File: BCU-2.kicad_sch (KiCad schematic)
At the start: 9 parts, among them J2 Conn_01x12_Male, J6 Conn_01x04_Male, U1 Teensy3.2

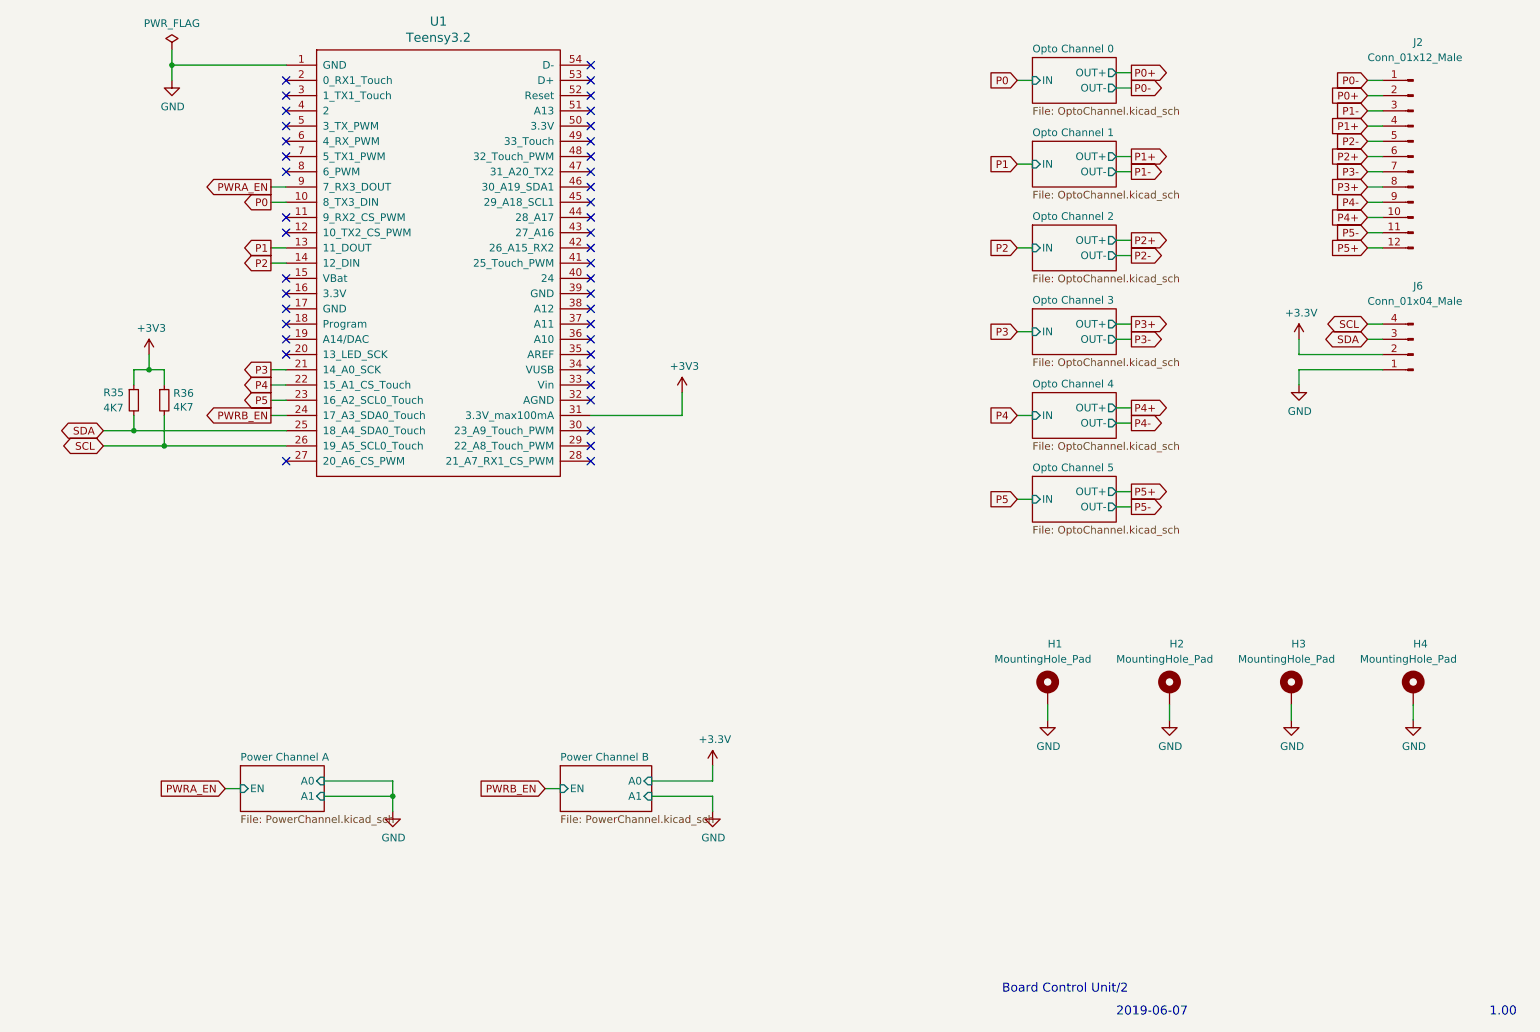
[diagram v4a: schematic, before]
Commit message: Schematic: Replace Teensy 3.2 by PCF8574
Signed-off-by: Geert Uytterhoeven <geert@linux-m68k.org>
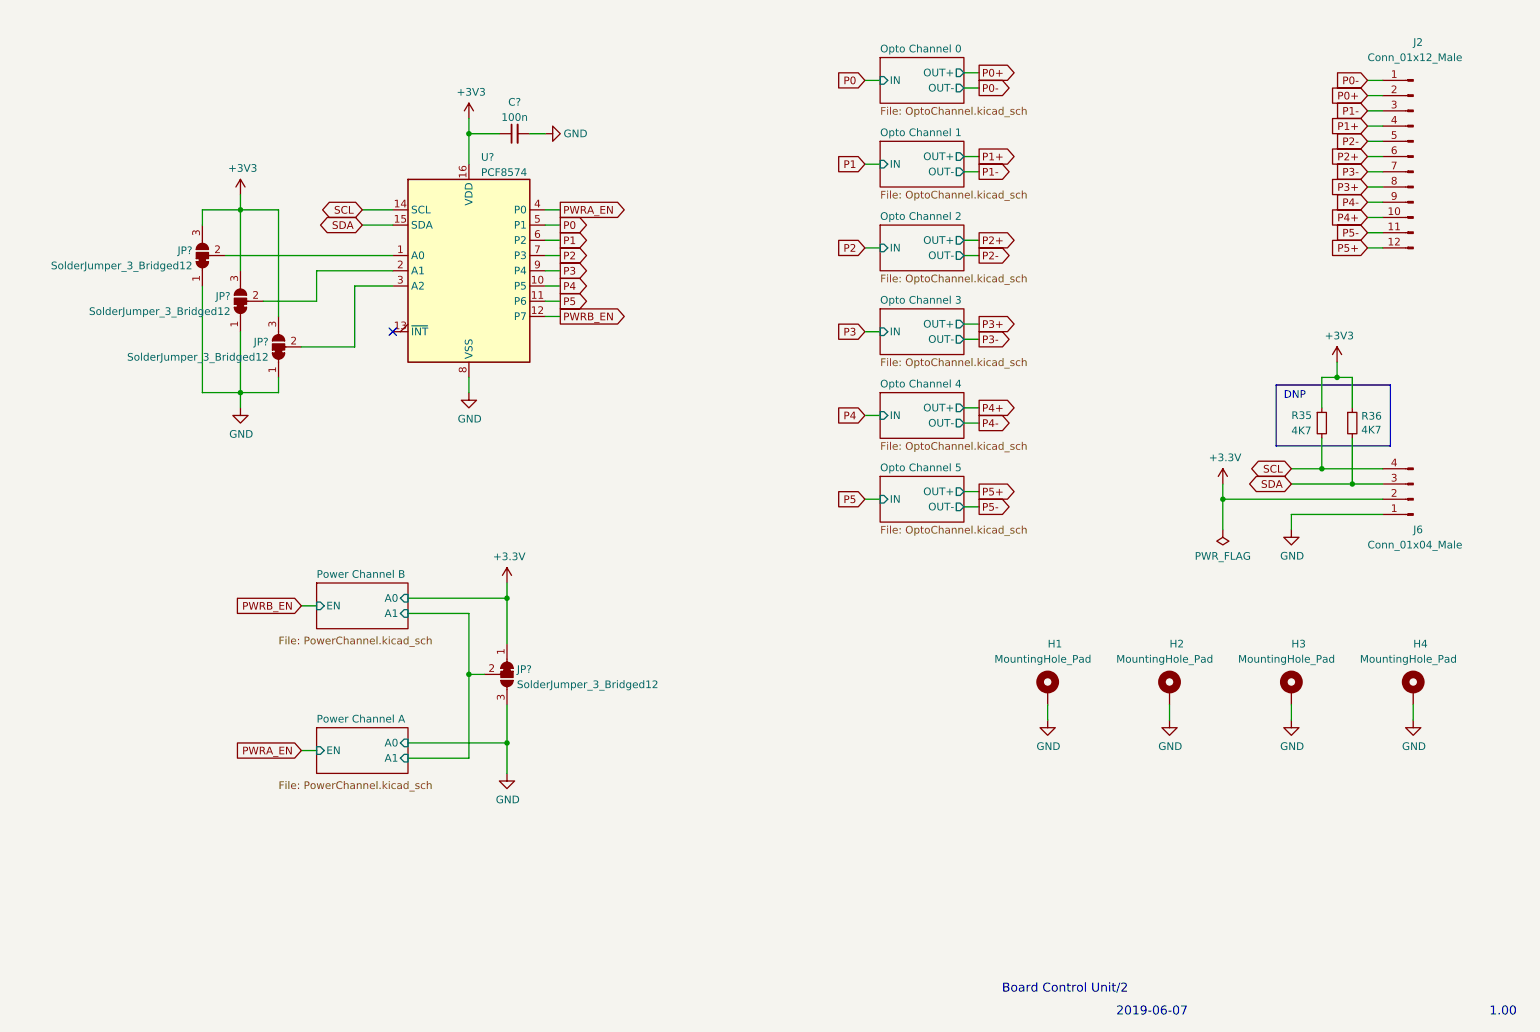
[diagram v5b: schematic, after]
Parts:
- removed U1: Teensy3.2, teensy:Teensy32-DIP28, symbol teensy:Teensy3.2
- added C?: 100n, Capacitor_SMD:C_0603_1608Metric_Pad1.05x0.95mm_HandSolder, symbol Device:C_Small
- added JP? (x4): SolderJumper_3_Bridged12, symbol Jumper:SolderJumper_3_Bridged12
- added U?: PCF8574, symbol Interface_Expansion:PCF8574
- R35, R36: now left out of the parts list
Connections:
- net +3V3: now also C?.1, JP?.1 (A), JP?.3 (B), JP?.3 (B), JP?.3 (B), U?.16 (VDD)
- net GND: now also C?.2, JP?.1 (A), JP?.1 (A), JP?.1 (A), JP?.3 (B), U?.8 (VSS)
- net P0: now also U?.5 (P1)
- net P1: now also U?.6 (P2)
- net P2: now also U?.7 (P3)
- net P3: now also U?.9 (P4)
- net P4: now also U?.10 (P5)
- net P5: now also U?.11 (P6)
- net PWRA_EN: now also U?.4 (P0)
- net PWRB_EN: now also U?.12 (P7)
- net SCL: now also R35.2, U?.14 (SCL); no longer R36.2
- net SDA: now also R36.2, U?.15 (SDA); no longer R35.2
- new net: JP?.2 (C), U?.1 (A0)
- new net: JP?.2 (C), U?.3 (A2)
- new net: JP?.2 (C), U?.2 (A1)
- new net Power Channel A/A1: JP?.2 (C)
- no-connect marks 42 -> 1
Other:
- note added: "DNP"
- moved on the sheet: J6, R35, R36

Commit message: Schematic: Renumber Power and Opto Channels
Renumber Power Channels to C-D, and Opto Channels to 6-11, to
avoid ambiguity with the channel numbers on the base BCU/2.

Signed-off-by: Geert Uytterhoeven <geert@linux-m68k.org>
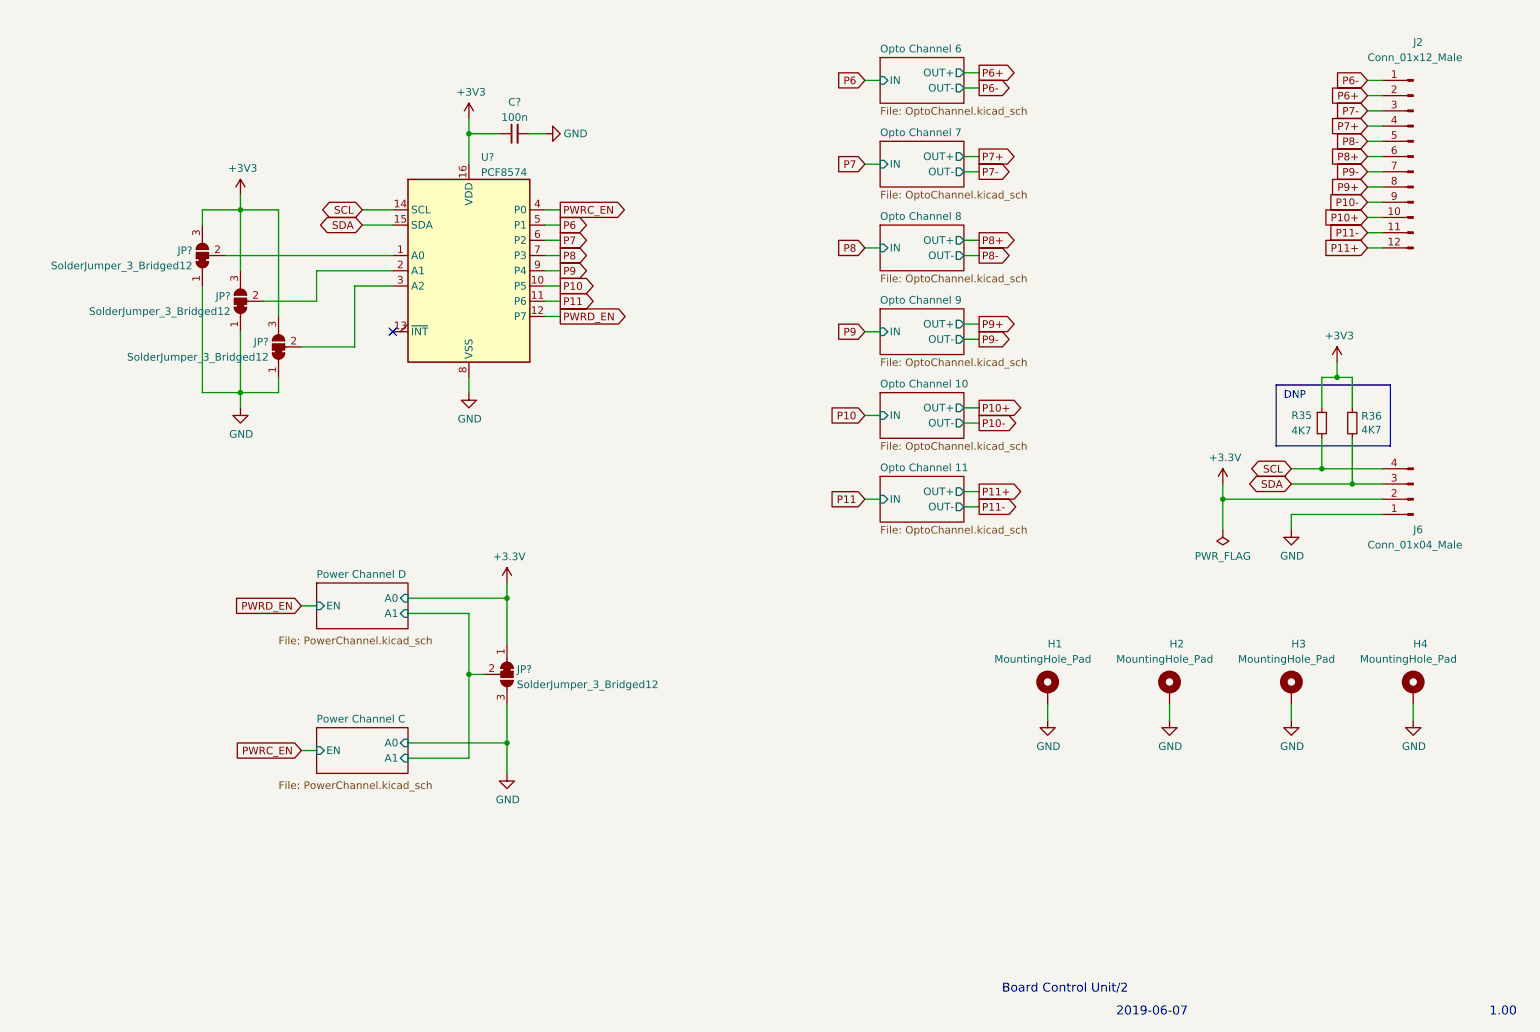
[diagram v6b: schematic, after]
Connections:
- net P0 renamed P6
- net P0+ renamed P6+
- net P0- renamed P6-
- net P1 renamed P7
- net P1+ renamed P7+
- net P1- renamed P7-
- net P2 renamed P8
- net P2+ renamed P8+
- net P2- renamed P8-
- net P3 renamed P9
- net P3+ renamed P9+
- net P3- renamed P9-
- net P4 renamed P10
- net P4+ renamed P10+
- net P4- renamed P10-
- net P5 renamed P11
- net P5+ renamed P11+
- net P5- renamed P11-
- net PWRA_EN renamed PWRC_EN
- net PWRB_EN renamed PWRD_EN
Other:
- sheet Opto Channel 0 renamed Opto Channel 6
- sheet Opto Channel 1 renamed Opto Channel 7
- sheet Opto Channel 2 renamed Opto Channel 8
- sheet Opto Channel 3 renamed Opto Channel 9
- sheet Opto Channel 4 renamed Opto Channel 10
- sheet Opto Channel 5 renamed Opto Channel 11
- sheet Power Channel A renamed Power Channel C
- sheet Power Channel B renamed Power Channel D

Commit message: Schematic: Annotate symbol references
Fill in schematic symbol reference designators.

Signed-off-by: Geert Uytterhoeven <geert@linux-m68k.org>
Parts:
- gave numbers to parts that had none: 6
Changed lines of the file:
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@@
   (symbol (lib_id "Jumper:SolderJumper_3_Bridged12") (at 105.41 137.16 270) (unit 1)
     (in_bom yes) (on_board yes) (fields_autoplaced)
-    (property "Reference" "JP?" (id 0) (at 107.061 136.3253 90)
+    (property "Reference" "JP4" (id 0) (at 107.061 136.3253 90)
       (effects (font (size 1.27 1.27)) (justify left))
     )
@@
   (symbol (lib_id "Jumper:SolderJumper_3_Bridged12") (at 54.61 67.31 90) (unit 1)
     (in_bom yes) (on_board yes) (fields_autoplaced)
-    (property "Reference" "JP?" (id 0) (at 52.9591 66.4753 90)
+    (property "Reference" "JP1" (id 0) (at 52.9591 66.4753 90)
       (effects (font (size 1.27 1.27)) (justify left))
     )
@@
   (symbol (lib_id "power:GND") (at 60.96 92.71 0) (unit 1)
     (in_bom yes) (on_board yes)
-    (property "Reference" "#PWR?" (id 0) (at 60.96 99.06 0)
+    (property "Reference" "#PWR02" (id 0) (at 60.96 99.06 0)
       (effects (font (size 1.27 1.27)) hide)
     )
@@
   (symbol (lib_id "power:GND") (at 111.76 46.99 90) (unit 1)
     (in_bom yes) (on_board yes)
-    (property "Reference" "#PWR?" (id 0) (at 118.11 46.99 0)
+    (property "Reference" "#PWR010" (id 0) (at 118.11 46.99 0)
       (effects (font (size 1.27 1.27)) hide)
     )
@@
   (symbol (lib_id "power:+3V3") (at 60.96 57.15 0) (unit 1)
     (in_bom yes) (on_board yes)
-    (property "Reference" "#PWR?" (id 0) (at 60.96 60.96 0)
+    (property "Reference" "#PWR01" (id 0) (at 60.96 60.96 0)
       (effects (font (size 1.27 1.27)) hide)
     )
@@
   (symbol (lib_id "Jumper:SolderJumper_3_Bridged12") (at 67.31 82.55 90) (unit 1)
     (in_bom yes) (on_board yes) (fields_autoplaced)
-    (property "Reference" "JP?" (id 0) (at 65.6591 81.7153 90)
+    (property "Reference" "JP3" (id 0) (at 65.6591 81.7153 90)
       (effects (font (size 1.27 1.27)) (justify left))
     )
@@
   (symbol (lib_id "Interface_Expansion:PCF8574") (at 99.06 69.85 0) (unit 1)
     (in_bom yes) (on_board yes) (fields_autoplaced)
-    (property "Reference" "U?" (id 0) (at 101.0794 50.9102 0)
+    (property "Reference" "U1" (id 0) (at 101.0794 50.9102 0)
       (effects (font (size 1.27 1.27)) (justify left))
     )
@@
   (symbol (lib_id "power:+3.3V") (at 105.41 121.92 0) (unit 1)
     (in_bom yes) (on_board yes)
-    (property "Reference" "#PWR?" (id 0) (at 105.41 125.73 0)
+    (property "Reference" "#PWR06" (id 0) (at 105.41 125.73 0)
       (effects (font (size 1.27 1.27)) hide)
     )
@@
   (symbol (lib_id "Device:C_Small") (at 106.68 46.99 90) (unit 1)
     (in_bom yes) (on_board yes) (fields_autoplaced)
-    (property "Reference" "C?" (id 0) (at 106.6863 41.7281 90))
+    (property "Reference" "C1" (id 0) (at 106.6863 41.7281 90))
     (property "Value" "100n" (id 1) (at 106.6863 44.265 90))
     (property "Footprint" "Capacitor_SMD:C_0603_1608Metric_Pad1.05x0.95mm_HandSolder" (id 2) (at 106.68 46.99 0)
@@
   (symbol (lib_id "power:GND") (at 99.06 90.17 0) (unit 1)
     (in_bom yes) (on_board yes)
-    (property "Reference" "#PWR?" (id 0) (at 99.06 96.52 0)
+    (property "Reference" "#PWR03" (id 0) (at 99.06 96.52 0)
       (effects (font (size 1.27 1.27)) hide)
     )
@@
   (symbol (lib_id "Jumper:SolderJumper_3_Bridged12") (at 60.96 74.93 90) (unit 1)
     (in_bom yes) (on_board yes) (fields_autoplaced)
-    (property "Reference" "JP?" (id 0) (at 59.3091 74.0953 90)
+    (property "Reference" "JP2" (id 0) (at 59.3091 74.0953 90)
       (effects (font (size 1.27 1.27)) (justify left))
     )
@@
       (reference "#FLG0101") (unit 1) (value "PWR_FLAG") (footprint "")
     )
+    (path "/b101e671-1882-4363-b7e6-51d4d4c68639"
+      (reference "#PWR01") (unit 1) (value "+3V3") (footprint "")
+    )
+    (path "/84b85743-219c-4961-b45d-b0e1fb054317"
+      (reference "#PWR02") (unit 1) (value "GND") (footprint "")
+    )
+    (path "/dc9888b8-5fc1-4a7b-b43b-f84d5eb0adaa"
+      (reference "#PWR03") (unit 1) (value "GND") (footprint "")
+    )
     (path "/00000000-0000-0000-0000-00005bbe1aa7"
       (reference "#PWR04") (unit 1) (value "+3V3") (footprint "")
@@
       (reference "#PWR05") (unit 1) (value "+3V3") (footprint "")
     )
+    (path "/d301f807-ce11-4903-86b4-814811ea43be"
+      (reference "#PWR06") (unit 1) (value "+3.3V") (footprint "")
+    )
     (path "/00000000-0000-0000-0000-00005be8d10d/00000000-0000-0000-0000-00005be8d423"
       (reference "#PWR07") (unit 1) (value "+3V3") (footprint "")
@@
       (reference "#PWR09") (unit 1) (value "GND") (footprint "")
     )
+    (path "/940cd4e4-73a2-49e9-9314-1a4ec55b2abb"
+      (reference "#PWR010") (unit 1) (value "GND") (footprint "")
+    )
     (path "/00000000-0000-0000-0000-00005be9e6f8/00000000-0000-0000-0000-00005be8d423"
       (reference "#PWR011") (unit 1) (value "+3V3") (footprint "")
@@
       (reference "#PWR018") (unit 1) (value "+3V3") (footprint "")
     )
+    (path "/00000000-0000-0000-0000-00005be8d10d/af7cc6d7-793b-4487-b233-b47678b4d967"
+      (reference "#PWR019") (unit 1) (value "+3V3") (footprint "")
+    )
+    (path "/00000000-0000-0000-0000-00005be9e6f8/af7cc6d7-793b-4487-b233-b47678b4d967"
+      (reference "#PWR020") (unit 1) (value "+3V3") (footprint "")
+    )
     (path "/00000000-0000-0000-0000-00005ce201a1"
       (reference "#PWR023") (unit 1) (value "+3.3V") (footprint "")
@@
       (reference "#PWR0112") (unit 1) (value "+3V3") (footprint "")
     )
-    (path "/84b85743-219c-4961-b45d-b0e1fb054317"
-      (reference "#PWR?") (unit 1) (value "GND") (footprint "")
-    )
-    (path "/940cd4e4-73a2-49e9-9314-1a4ec55b2abb"
-      (reference "#PWR?") (unit 1) (value "GND") (footprint "")
-    )
-    (path "/00000000-0000-0000-0000-00005be9e6f8/af7cc6d7-793b-4487-b233-b47678b4d967"
-      (reference "#PWR?") (unit 1) (value "+3V3") (footprint "")
-    )
-    (path "/00000000-0000-0000-0000-00005be8d10d/af7cc6d7-793b-4487-b233-b47678b4d967"
-      (reference "#PWR?") (unit 1) (value "+3V3") (footprint "")
-    )
-    (path "/b101e671-1882-4363-b7e6-51d4d4c68639"
-      (reference "#PWR?") (unit 1) (value "+3V3") (footprint "")
-    )
-    (path "/d301f807-ce11-4903-86b4-814811ea43be"
-      (reference "#PWR?") (unit 1) (value "+3.3V") (footprint "")
-    )
-    (path "/dc9888b8-5fc1-4a7b-b43b-f84d5eb0adaa"
-      (reference "#PWR?") (unit 1) (value "GND") (footprint "")
+    (path "/d939b064-8985-4b7d-8a1a-0577d1e8851f"
+      (reference "C1") (unit 1) (value "100n") (footprint "Capacitor_SMD:C_0603_1608Metric_Pad1.05x0.95mm_HandSolder")
     )
     (path "/00000000-0000-0000-0000-00005be8d10d/00000000-0000-0000-0000-00005ce3761d"
@@
       (reference "C12") (unit 1) (value "10µ") (footprint "Capacitor_SMD:C_0805_2012Metric_Pad1.15x1.40mm_HandSolder")
     )
-    (path "/d939b064-8985-4b7d-8a1a-0577d1e8851f"
-      (reference "C?") (unit 1) (value "100n") (footprint "Capacitor_SMD:C_0603_1608Metric_Pad1.05x0.95mm_HandSolder")
-    )
     (path "/00000000-0000-0000-0000-00005be4dd5e/00000000-0000-0000-0000-00005be627f1"
       (reference "D3") (unit 1) (value "Yellow") (footprint "LED_SMD:LED_0603_1608Metric_Castellated")
@@
       (reference "J6") (unit 1) (value "Conn_01x04_Male") (footprint "Connector_JST:JST_PH_B4B-PH-K_1x04_P2.00mm_Vertical")
     )
+    (path "/2874d169-00ca-4711-b820-9bd76daabb8e"
+      (reference "JP1") (unit 1) (value "SolderJumper_3_Bridged12") (footprint "")
+    )
+    (path "/f20bea7b-9aea-47e6-889a-0fdfeb98c0ab"
+      (reference "JP2") (unit 1) (value "SolderJumper_3_Bridged12") (footprint "")
+    )
+    (path "/c61569ba-e093-4c18-ad24-56dd1bfafc07"
+      (reference "JP3") (unit 1) (value "SolderJumper_3_Bridged12") (footprint "")
+    )
     (path "/250e396e-532b-403e-9923-ba97292ccd93"
-      (reference "JP?") (unit 1) (value "SolderJumper_3_Bridged12") (footprint "")
-    )
-    (path "/2874d169-00ca-4711-b820-9bd76daabb8e"
-      (reference "JP?") (unit 1) (value "SolderJumper_3_Bridged12") (footprint "")
-    )
-    (path "/c61569ba-e093-4c18-ad24-56dd1bfafc07"
-      (reference "JP?") (unit 1) (value "SolderJumper_3_Bridged12") (footprint "")
-    )
-    (path "/f20bea7b-9aea-47e6-889a-0fdfeb98c0ab"
-      (reference "JP?") (unit 1) (value "SolderJumper_3_Bridged12") (footprint "")
+      (reference "JP4") (unit 1) (value "SolderJumper_3_Bridged12") (footprint "")
     )
     (path "/00000000-0000-0000-0000-00005be8d10d/00000000-0000-0000-0000-00005bf70897"
@@
       (reference "R36") (unit 1) (value "4K7") (footprint "Resistor_SMD:R_0603_1608Metric_Pad1.05x0.95mm_HandSolder")
     )
+    (path "/ca56c6fa-1c9a-4c18-af31-0eba468c8eab"
+      (reference "U1") (unit 1) (value "PCF8574") (footprint "")
+    )
     (path "/00000000-0000-0000-0000-00005be4dd5e/00000000-0000-0000-0000-00005be62801"
       (reference "U2") (unit 1) (value "HCPL-181") (footprint "Package_DIP:SMDIP-4_W7.62mm")
@@
       (reference "U13") (unit 1) (value "INA219xID") (footprint "Package_SO:SOIC-8_3.9x4.9mm_P1.27mm")
     )
-    (path "/ca56c6fa-1c9a-4c18-af31-0eba468c8eab"
-      (reference "U?") (unit 1) (value "PCF8574") (footprint "")
-    )
-  )
+  )
